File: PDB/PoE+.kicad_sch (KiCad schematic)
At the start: 13 parts, among them IC1 TPS23861PWR, J15 RJ45_Abracon_ARJP11A-MASA-B-A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, Q9 CSD19538Q3AT

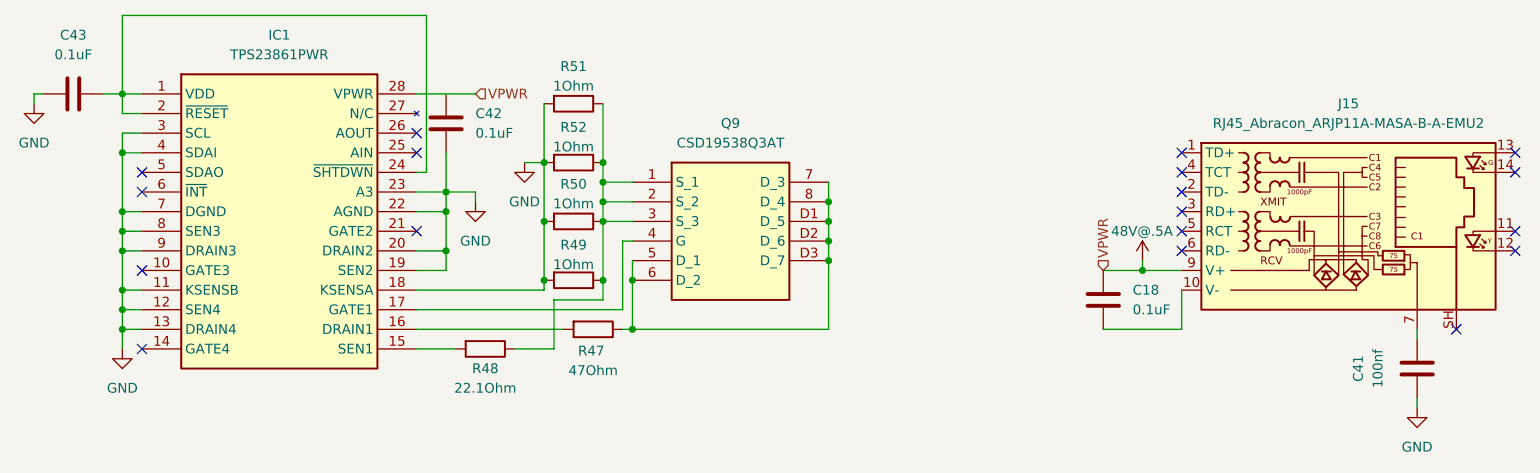
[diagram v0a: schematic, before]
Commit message: finished PoE+
the negotiation circuit should be good now but needs the I2C connection still
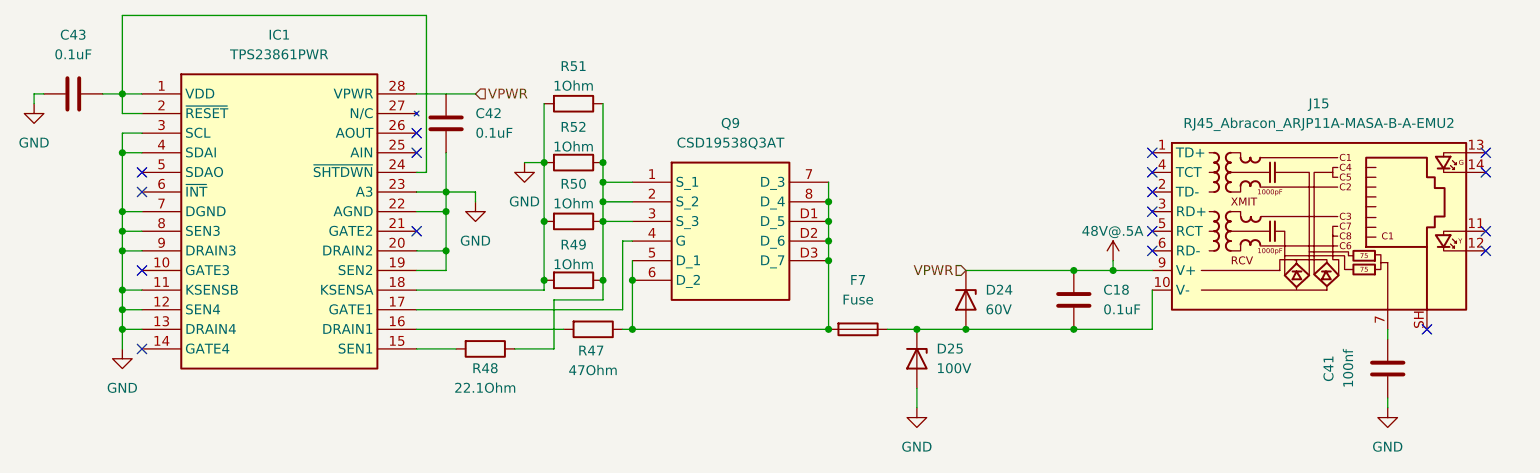
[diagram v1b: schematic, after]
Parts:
- added D24: 60V, symbol Device:D_Zener
- added D25: 100V, symbol Device:D_Zener
- added F7: Fuse, symbol Device:Fuse
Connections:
- net 48V@.5A: now also D24.1 (K)
- net GND: now also D25.2 (A)
- net at Q9.5 (D_1), Q9.6 (D_2), Q9.7 (D_3)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: now also F7.2
- net at C18.2, J15.10 (V-): now also D24.2 (A), D25.1 (K), F7.1
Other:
- moved on the sheet: C18, C41, J15

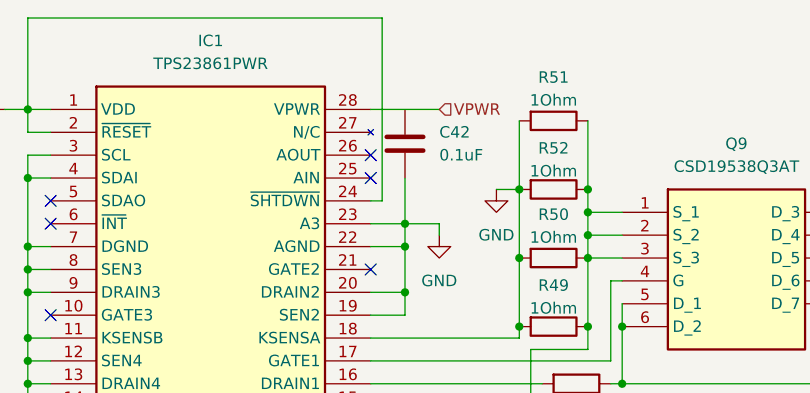
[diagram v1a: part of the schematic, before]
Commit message: updated footprints
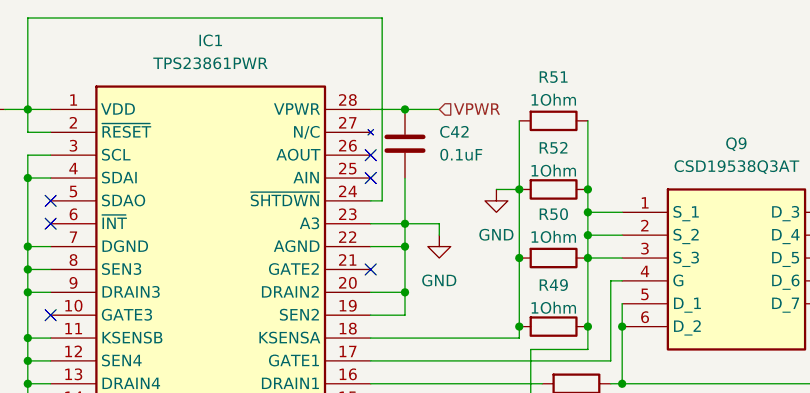
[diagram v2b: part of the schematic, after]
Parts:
- C42, C43: footprint (none) -> Capacitor_SMD:C_0603_1608Metric
- F7: footprint (none) -> Fuse:Fuse_1206_3216Metric
- R49, R50, R51, R52: footprint (none) -> Resistor_SMD:R_0603_1608Metric
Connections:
- net 48V@.5A: now also C42.2
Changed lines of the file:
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@@
+	)
+	(junction
+		(at 109.22 74.93)
+		(diameter 0)
+		(color 0 0 0 0)
 	)
 	(junction
@@
 	(wire
 		(pts
+			(xy 109.22 74.93) (xy 113.03 74.93)
+		)
+		(stroke
+			(width 0)
+			(type default)
+		)
+	)
+	(wire
+		(pts
 			(xy 200.66 100.33) (xy 200.66 105.41)
 		)
@@
 	(wire
 		(pts
-			(xy 105.41 74.93) (xy 113.03 74.93)
+			(xy 105.41 74.93) (xy 109.22 74.93)
 		)
 		(stroke
@@
 			)
 		)
-		(property "Footprint" ""
+		(property "Footprint" "Capacitor_SMD:C_0603_1608Metric"
 			(at 108.2548 74.93 0)
 			(hide yes)
@@
 			)
 		)
-		(property "Footprint" ""
+		(property "Footprint" "Resistor_SMD:R_0603_1608Metric"
 			(at 125.73 89.662 90)
 			(hide yes)
@@
 			)
 		)
-		(property "Footprint" ""
+		(property "Footprint" "Resistor_SMD:R_0603_1608Metric"
 			(at 125.73 97.282 90)
 			(hide yes)
@@
 			)
 		)
-		(property "Footprint" ""
+		(property "Footprint" "Capacitor_SMD:C_0603_1608Metric"
 			(at 57.15 75.8952 0)
 			(hide yes)
@@
 			)
 		)
-		(property "Footprint" ""
+		(property "Footprint" "Fuse:Fuse_1206_3216Metric"
 			(at 162.56 103.632 90)
 			(hide yes)
@@
 			)
 		)
-		(property "Footprint" ""
+		(property "Footprint" "Resistor_SMD:R_0603_1608Metric"
 			(at 125.73 74.422 90)
 			(hide yes)
@@
 			)
 		)
-		(property "Footprint" ""
+		(property "Footprint" "Resistor_SMD:R_0603_1608Metric"
 			(at 125.73 82.042 90)
 			(hide yes)

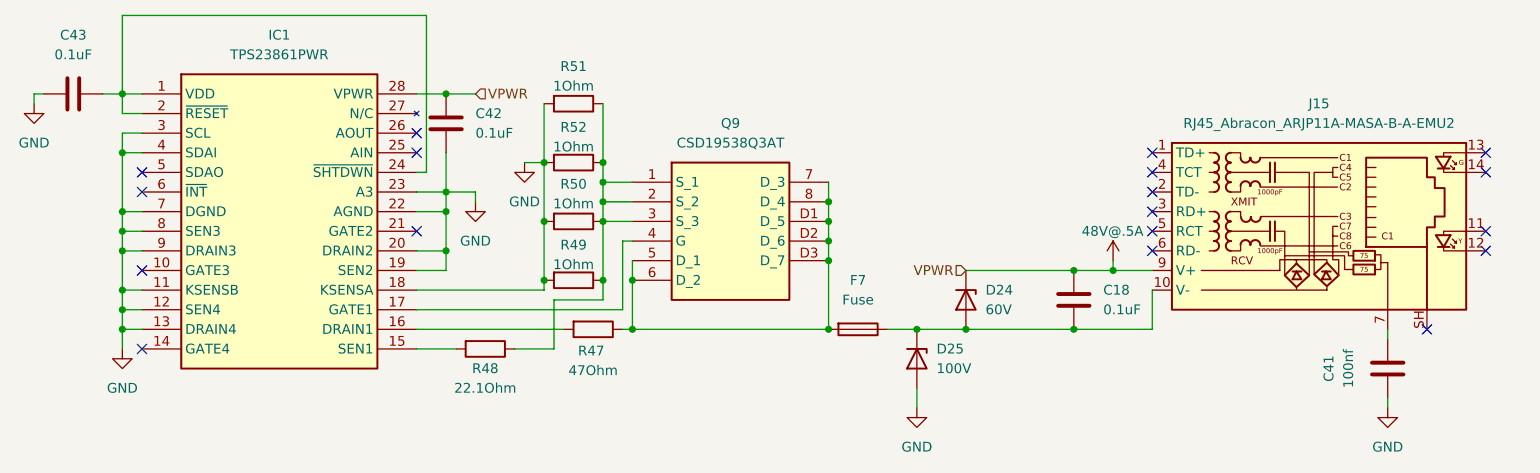
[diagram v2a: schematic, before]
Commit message: coordinated labels in schem
Labeled all components to be Rxx, Cxx, ext forms through all sheets so labels for BOM and layout are work together as one long list.
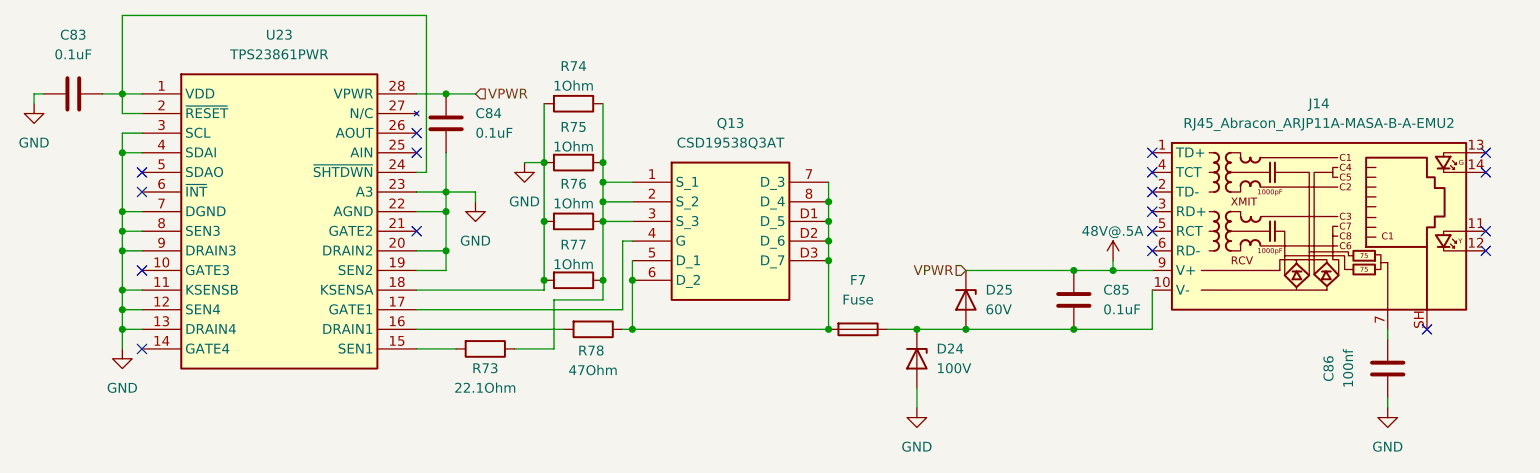
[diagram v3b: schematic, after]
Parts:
- renumbered C43 to C83, C42 to C84, C18 to C85, C41 to C86, D25 to D24, D24 to D25, J15 to J14, Q9 to Q13, R48 to R73, R51 to R74, R52 to R75, R50 to R76, R49 to R77, R47 to R78, IC1 to U23
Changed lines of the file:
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@@
 		(dnp no)
 		(fields_autoplaced yes)
-		(property "Reference" "C41"
+		(property "Reference" "C86"
 			(at 223.52 110.49 90)
 			(show_name no)
@@
 			(project "PDB"
 				(path "/a9cf05c4-aac5-4cf1-b700-1d3045f8dfbd/0ca8fca8-7872-4a37-82ca-cc32f4883a53"
-					(reference "C41")
+					(reference "C86")
 					(unit 1)
 				)
@@
 		(dnp no)
 		(fields_autoplaced yes)
-		(property "Reference" "#PWR069"
+		(property "Reference" "#PWR0101"
 			(at 113.03 95.25 0)
 			(hide yes)
@@
 			(project "PDB"
 				(path "/a9cf05c4-aac5-4cf1-b700-1d3045f8dfbd/0ca8fca8-7872-4a37-82ca-cc32f4883a53"
-					(reference "#PWR069")
+					(reference "#PWR0101")
 					(unit 1)
 				)
@@
 		(dnp no)
 		(fields_autoplaced yes)
-		(property "Reference" "C42"
+		(property "Reference" "C84"
 			(at 113.03 77.4699 0)
 			(show_name no)
@@
 			(project "PDB"
 				(path "/a9cf05c4-aac5-4cf1-b700-1d3045f8dfbd/0ca8fca8-7872-4a37-82ca-cc32f4883a53"
-					(reference "C42")
+					(reference "C84")
 					(unit 1)
 				)
@@
 		(in_pos_files yes)
 		(dnp no)
-		(property "Reference" "#PWR067"
+		(property "Reference" "#PWR0104"
 			(at 195.58 100.33 0)
 			(hide yes)
@@
 			(project "PDB"
 				(path "/a9cf05c4-aac5-4cf1-b700-1d3045f8dfbd/0ca8fca8-7872-4a37-82ca-cc32f4883a53"
-					(reference "#PWR067")
+					(reference "#PWR0104")
 					(unit 1)
 				)
@@
 		(dnp no)
 		(fields_autoplaced yes)
-		(property "Reference" "#PWR0103"
+		(property "Reference" "#PWR099"
 			(at 55.88 82.55 0)
 			(hide yes)
@@
 			(project "PDB"
 				(path "/a9cf05c4-aac5-4cf1-b700-1d3045f8dfbd/0ca8fca8-7872-4a37-82ca-cc32f4883a53"
-					(reference "#PWR0103")
+					(reference "#PWR099")
 					(unit 1)
 				)
@@
 		(in_pos_files yes)
 		(dnp no)
-		(property "Reference" "R50"
+		(property "Reference" "R76"
 			(at 125.73 86.614 90)
 			(show_name no)
@@
 			(project "PDB"
 				(path "/a9cf05c4-aac5-4cf1-b700-1d3045f8dfbd/0ca8fca8-7872-4a37-82ca-cc32f4883a53"
-					(reference "R50")
+					(reference "R76")
 					(unit 1)
 				)
@@
 		(dnp no)
 		(fields_autoplaced yes)
-		(property "Reference" "D24"
+		(property "Reference" "D25"
 			(at 179.07 100.3299 90)
 			(show_name no)
@@
 			(project "PDB"
 				(path "/a9cf05c4-aac5-4cf1-b700-1d3045f8dfbd/0ca8fca8-7872-4a37-82ca-cc32f4883a53"
-					(reference "D24")
+					(reference "D25")
 					(unit 1)
 				)
@@
 		(dnp no)
 		(fields_autoplaced yes)
-		(property "Reference" "#PWR0104"
+		(property "Reference" "#PWR0103"
 			(at 170.18 121.92 0)
 			(hide yes)
@@
 			(project "PDB"
 				(path "/a9cf05c4-aac5-4cf1-b700-1d3045f8dfbd/0ca8fca8-7872-4a37-82ca-cc32f4883a53"
-					(reference "#PWR0104")
+					(reference "#PWR0103")
 					(unit 1)
 				)
@@
 		(in_pos_files yes)
 		(dnp no)
-		(property "Reference" "R49"
+		(property "Reference" "R77"
 			(at 125.73 94.488 90)
 			(show_name no)
@@
 			(project "PDB"
 				(path "/a9cf05c4-aac5-4cf1-b700-1d3045f8dfbd/0ca8fca8-7872-4a37-82ca-cc32f4883a53"
-					(reference "R49")
+					(reference "R77")
 					(unit 1)
 				)
@@
 		(dnp no)
 		(fields_autoplaced yes)
-		(property "Reference" "C43"
+		(property "Reference" "C83"
 			(at 60.96 67.31 90)
 			(show_name no)
@@
 			(project "PDB"
 				(path "/a9cf05c4-aac5-4cf1-b700-1d3045f8dfbd/0ca8fca8-7872-4a37-82ca-cc32f4883a53"
-					(reference "C43")
+					(reference "C83")
 					(unit 1)
 				)
@@
 		(in_pos_files yes)
 		(dnp no)
-		(property "Reference" "R47"
+		(property "Reference" "R78"
 			(at 128.016 108.204 90)
 			(show_name no)
@@
 			(project "PDB"
 				(path "/a9cf05c4-aac5-4cf1-b700-1d3045f8dfbd/0ca8fca8-7872-4a37-82ca-cc32f4883a53"
-					(reference "R47")
+					(reference "R78")
 					(unit 1)
 				)
@@
 		(dnp no)
 		(fields_autoplaced yes)
-		(property "Reference" "#PWR0101"
+		(property "Reference" "#PWR0105"
 			(at 231.14 121.92 0)
 			(hide yes)
@@
 			(project "PDB"
 				(path "/a9cf05c4-aac5-4cf1-b700-1d3045f8dfbd/0ca8fca8-7872-4a37-82ca-cc32f4883a53"
-					(reference "#PWR0101")
+					(reference "#PWR0105")
 					(unit 1)
 				)
@@
 		(dnp no)
 		(fields_autoplaced yes)
-		(property "Reference" "#PWR066"
+		(property "Reference" "#PWR0100"
 			(at 67.31 114.3 0)
 			(hide yes)
@@
 			(project "PDB"
 				(path "/a9cf05c4-aac5-4cf1-b700-1d3045f8dfbd/0ca8fca8-7872-4a37-82ca-cc32f4883a53"
-					(reference "#PWR066")
+					(reference "#PWR0100")
 					(unit 1)
 				)
@@
 		(in_pos_files yes)
 		(dnp no)
-		(property "Reference" "R51"
+		(property "Reference" "R74"
 			(at 125.73 71.374 90)
 			(show_name no)
@@
 			(project "PDB"
 				(path "/a9cf05c4-aac5-4cf1-b700-1d3045f8dfbd/0ca8fca8-7872-4a37-82ca-cc32f4883a53"
-					(reference "R51")
+					(reference "R74")
 					(unit 1)
 				)
@@
 		(dnp no)
 		(fields_autoplaced yes)
-		(property "Reference" "IC1"
+		(property "Reference" "U23"
 			(at 87.63 67.31 0)
 			(show_name no)
@@
 			(project "PDB"
 				(path "/a9cf05c4-aac5-4cf1-b700-1d3045f8dfbd/0ca8fca8-7872-4a37-82ca-cc32f4883a53"
-					(reference "IC1")
+					(reference "U23")
 					(unit 1)
 				)
@@
 		(dnp no)
 		(fields_autoplaced yes)
-		(property "Reference" "Q9"
+		(property "Reference" "Q13"
 			(at 146.05 78.74 0)
 			(show_name no)
@@
 			(project "PDB"
 				(path "/a9cf05c4-aac5-4cf1-b700-1d3045f8dfbd/0ca8fca8-7872-4a37-82ca-cc32f4883a53"
-					(reference "Q9")
+					(reference "Q13")
 					(unit 1)
 				)
@@
 		(in_pos_files yes)
 		(dnp no)
-		(property "Reference" "R48"
+		(property "Reference" "R73"
 			(at 114.3 110.49 90)
 			(show_name no)
@@
 			(project "PDB"
 				(path "/a9cf05c4-aac5-4cf1-b700-1d3045f8dfbd/0ca8fca8-7872-4a37-82ca-cc32f4883a53"
-					(reference "R48")
+					(reference "R73")
 					(unit 1)
 				)
@@
 		(dnp no)
 		(fields_autoplaced yes)
-		(property "Reference" "J15"
+		(property "Reference" "J14"
 			(at 222.25 76.2 0)
 			(show_name no)
@@
 			(project "PDB"
 				(path "/a9cf05c4-aac5-4cf1-b700-1d3045f8dfbd/0ca8fca8-7872-4a37-82ca-cc32f4883a53"
-					(reference "J15")
+					(reference "J14")
 					(unit 1)
 				)
@@
 		(dnp no)
 		(fields_autoplaced yes)
-		(property "Reference" "D25"
+		(property "Reference" "D24"
 			(at 172.72 107.9499 90)
 			(show_name no)
@@
 			(project "PDB"
 				(path "/a9cf05c4-aac5-4cf1-b700-1d3045f8dfbd/0ca8fca8-7872-4a37-82ca-cc32f4883a53"
-					(reference "D25")
+					(reference "D24")
 					(unit 1)
 				)
@@
 		(dnp no)
 		(fields_autoplaced yes)
-		(property "Reference" "C18"
+		(property "Reference" "C85"
 			(at 194.31 100.3299 0)
 			(show_name no)
@@
 			(project "PDB"
 				(path "/a9cf05c4-aac5-4cf1-b700-1d3045f8dfbd/0ca8fca8-7872-4a37-82ca-cc32f4883a53"
-					(reference "C18")
+					(reference "C85")
 					(unit 1)
 				)
@@
 		(in_pos_files yes)
 		(dnp no)
-		(property "Reference" "R52"
+		(property "Reference" "R75"
 			(at 125.73 79.248 90)
 			(show_name no)
@@
 			(project "PDB"
 				(path "/a9cf05c4-aac5-4cf1-b700-1d3045f8dfbd/0ca8fca8-7872-4a37-82ca-cc32f4883a53"
-					(reference "R52")
-					(unit 1)
-				)
+					(reference "R75")
+					(unit 1)
+				)

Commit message: last push before removing oring
i think we're going with an interlock system instead. the battery oring on here will take far too much physical room on the board to make it worthwhile. this push removes the oring and assumes a single power input.
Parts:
- Q13: footprint foot:CSD19538Q3AT -> CSD19538Q3AT
- U23: footprint foot:TPS23861PWR -> SOP65P640X120-28N
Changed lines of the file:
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@@
 			)
 		)
-		(property "Footprint" "foot:TPS23861PWR"
+		(property "Footprint" "SOP65P640X120-28N"
 			(at 101.6 169.85 0)
 			(hide yes)
@@
 			)
 		)
-		(property "Footprint" "foot:CSD19538Q3AT"
+		(property "Footprint" "CSD19538Q3AT"
 			(at 154.94 181.28 0)
 			(hide yes)
